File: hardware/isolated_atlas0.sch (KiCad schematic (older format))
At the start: 14 parts, among them J201 CONN_01X02, U201 adm3260, U202 ATLAS_SENSOR

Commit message: Fix SSOP-20 width on the isolator.
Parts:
- U201: footprint SMD_Packages:SSOP-20 -> conservify:SSOP20-53
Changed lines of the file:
@@
 F 0 "U201" H 4400 2750 60  0000 C CNN
 F 1 "adm3260" H 4400 2900 60  0000 C CNN
-F 2 "SMD_Packages:SSOP-20" H 4400 2900 60  0001 C CNN
+F 2 "conservify:SSOP20-53" H 4400 2900 60  0001 C CNN
 F 3 "" H 4400 2900 60  0001 C CNN
 F 4 "584-ADM3260ARSZ" H 0   0   50  0001 C CNN "spn1"

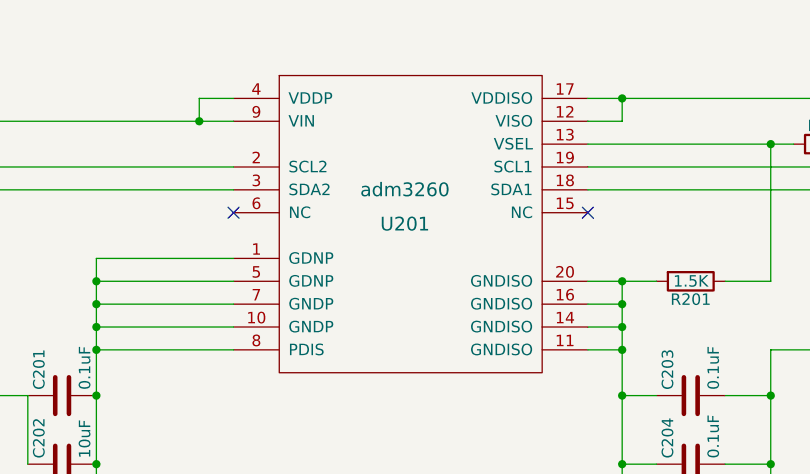
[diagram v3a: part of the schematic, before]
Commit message: Fixing some component names.
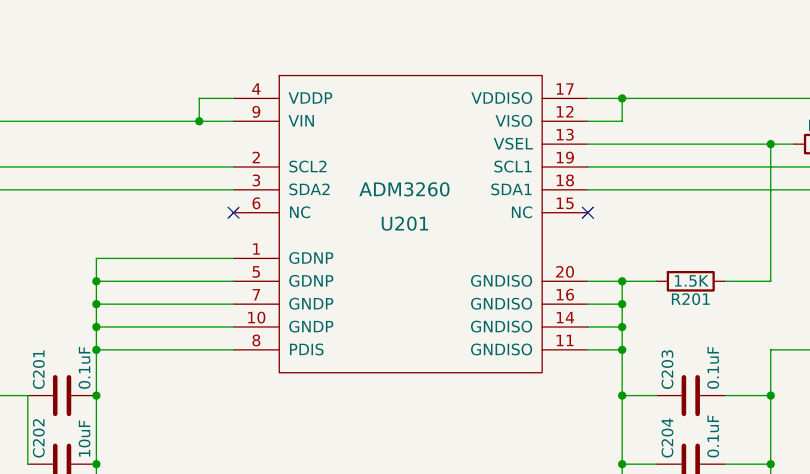
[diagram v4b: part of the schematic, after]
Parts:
- C201, C202, C203, C204, C205, C206, J201, R201, R202, R203, R204, R205, U202: price (none) -> 0
- U201: value adm3260 -> ADM3260; price (none) -> 0

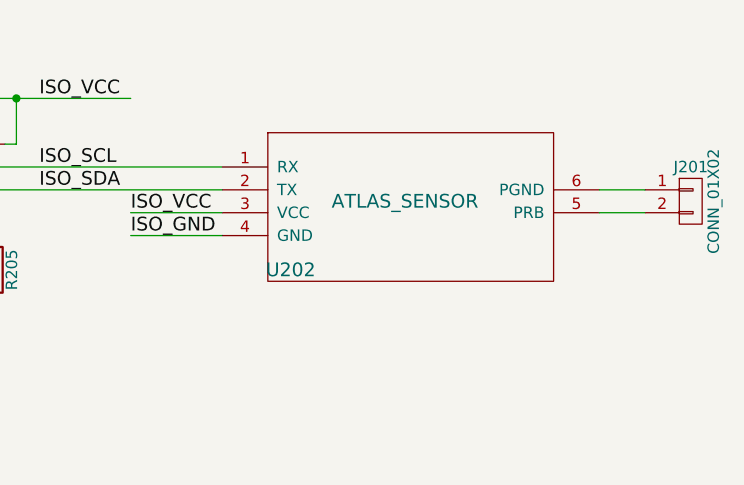
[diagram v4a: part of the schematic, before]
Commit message: Individual atlas sensor values for costing.
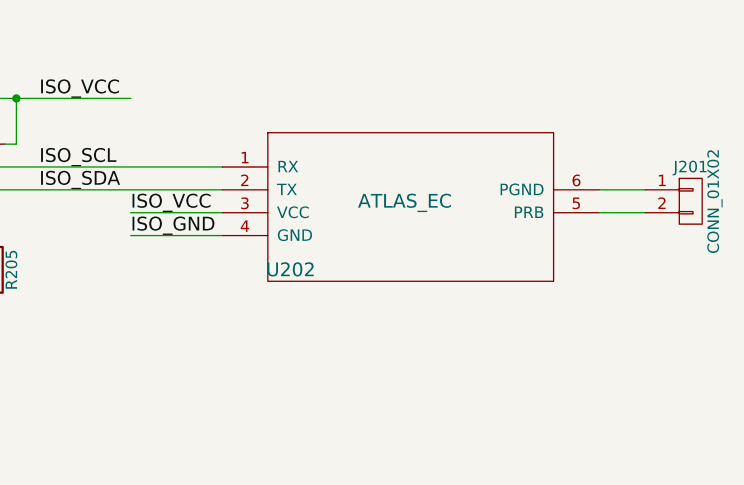
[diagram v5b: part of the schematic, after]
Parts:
- U202: value ATLAS_SENSOR -> ATLAS_EC

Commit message: Normalizing some passive footprints.
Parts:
- C201, C203, C204: footprint Resistors_SMD:R_0603_HandSoldering -> Capacitors_SMD:C_0603_HandSoldering
- C202, C205, C206: footprint Resistors_SMD:R_0603_HandSoldering -> Capacitors_SMD:C_0603_HandSoldering; spn1 810-C1608X7S0J106M -> 81-GRM188R60J106ME47

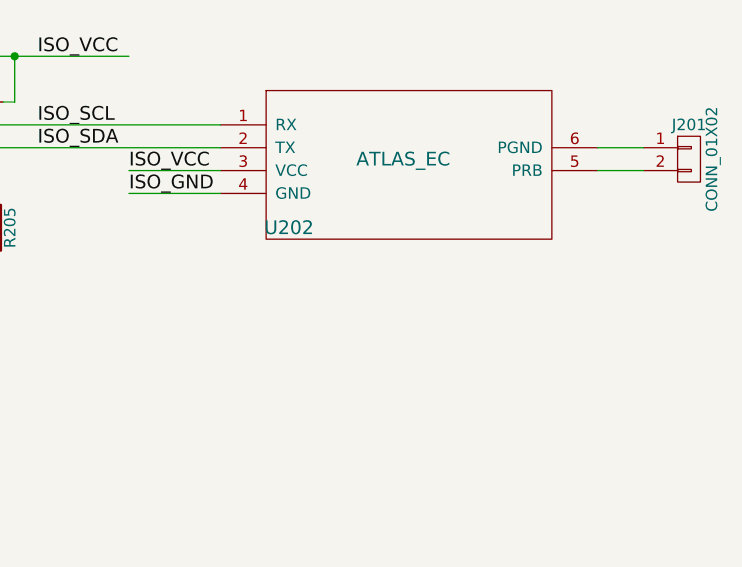
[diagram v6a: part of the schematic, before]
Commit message: Adding placeholders for probes for the BOM.
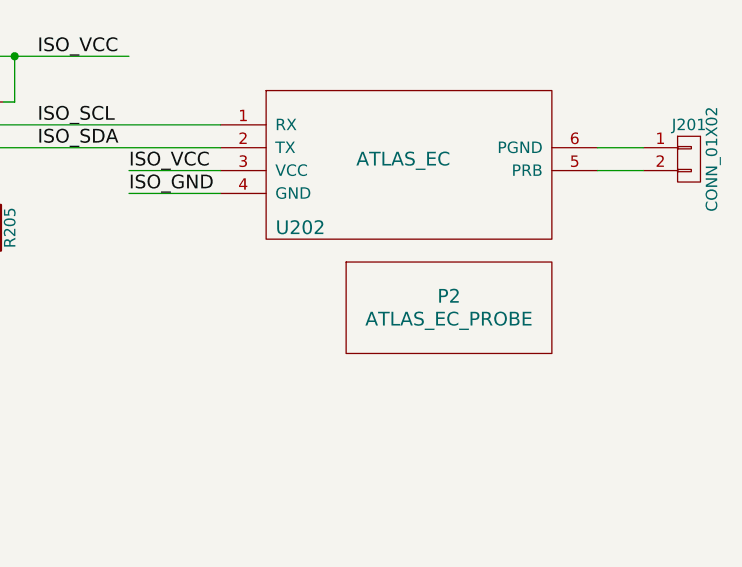
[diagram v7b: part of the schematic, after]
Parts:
- added P2: ATLAS_EC_PROBE, Oddities:Dummy_Empty, symbol WATER_PROBE

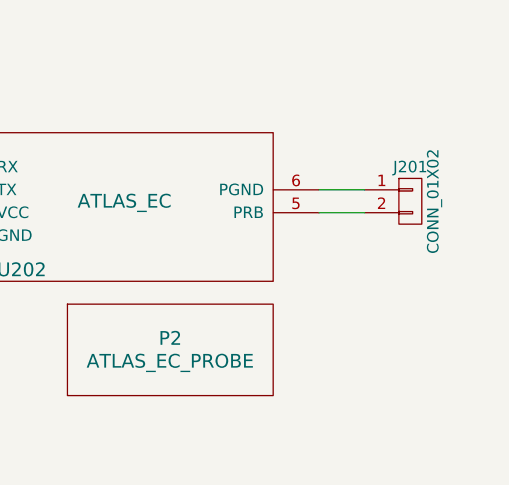
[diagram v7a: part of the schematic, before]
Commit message: Add footprint for OEM Atlas Circuit.
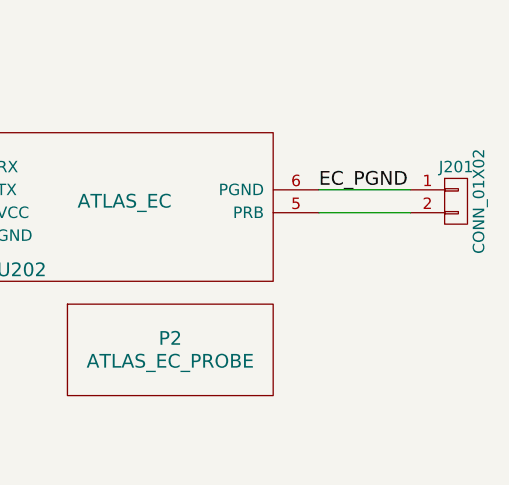
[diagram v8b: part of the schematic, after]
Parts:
- U202: footprint conservify:atlas_sensor_board -> conservify:ATLAS_SENSOR_BOARD_COMBO
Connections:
- net labels added: EC_PGND
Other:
- moved on the sheet: J201
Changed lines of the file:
@@
 F 0 "U202" H 8150 2550 60  0000 C CNN
 F 1 "ATLAS_EC" H 8600 2850 60  0000 C CNN
-F 2 "conservify:atlas_sensor_board" H 8550 2900 60  0001 C CNN
+F 2 "conservify:ATLAS_SENSOR_BOARD_COMBO" H 8550 2900 60  0001 C CNN
 F 3 "" H 8550 2900 60  0001 C CNN
 F 4 "0" H 8100 2650 50  0001 C CNN "price"
@@
 L CONN_01X02 J201
 U 1 1 59A1BC7B
-P 9850 2950
-F 0 "J201" H 9850 3100 50  0000 C CNN
-F 1 "CONN_01X02" V 9950 2950 50  0000 C CNN
-F 2 "conservify:BNC" H 9850 2950 50  0001 C CNN
-F 3 "" H 9850 2950 50  0001 C CNN
-F 4 "0" H 9850 3200 50  0001 C CNN "price"
-F 5 "523-31-5431" H 0   0   50  0001 C CNN "spn1"
-	1    9850 2950
+P 10050 2950
+F 0 "J201" H 10050 3100 50  0000 C CNN
+F 1 "CONN_01X02" V 10150 2950 50  0000 C CNN
+F 2 "conservify:BNC" H 10050 2950 50  0001 C CNN
+F 3 "" H 10050 2950 50  0001 C CNN
+F 4 "0" H 10050 3200 50  0001 C CNN "price"
+F 5 "523-31-5431" H 200 0   50  0001 C CNN "spn1"
+	1    10050 2950
 	1    0    0    -1
 $EndComp
@@
 	7400 3000 7800 3000
 Wire Wire Line
-	9450 2900 9650 2900
+	9450 2900 9850 2900
 Wire Wire Line
-	9650 3000 9450 3000
+	9450 3000 9850 3000
 Connection ~ 5350 3500
 Connection ~ 5350 3400
@@
 	1    0    0    -1
 $EndComp
+Text Label 9450 2900 0    60   ~ 0
+EC_PGND
 $EndSCHEMATC
